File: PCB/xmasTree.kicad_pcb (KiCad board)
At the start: 2 copper layers, 183.5 x 138.9 mm, 37 parts, among them J1 USB_B_Micro, J2 Conn_01x05, J3 Conn_01x05, J4 Conn_01x05, J5 Conn_01x04, Q1 BSS138, U1 LD1117S33TR_SOT223, U2 ESP32-WROOM-32

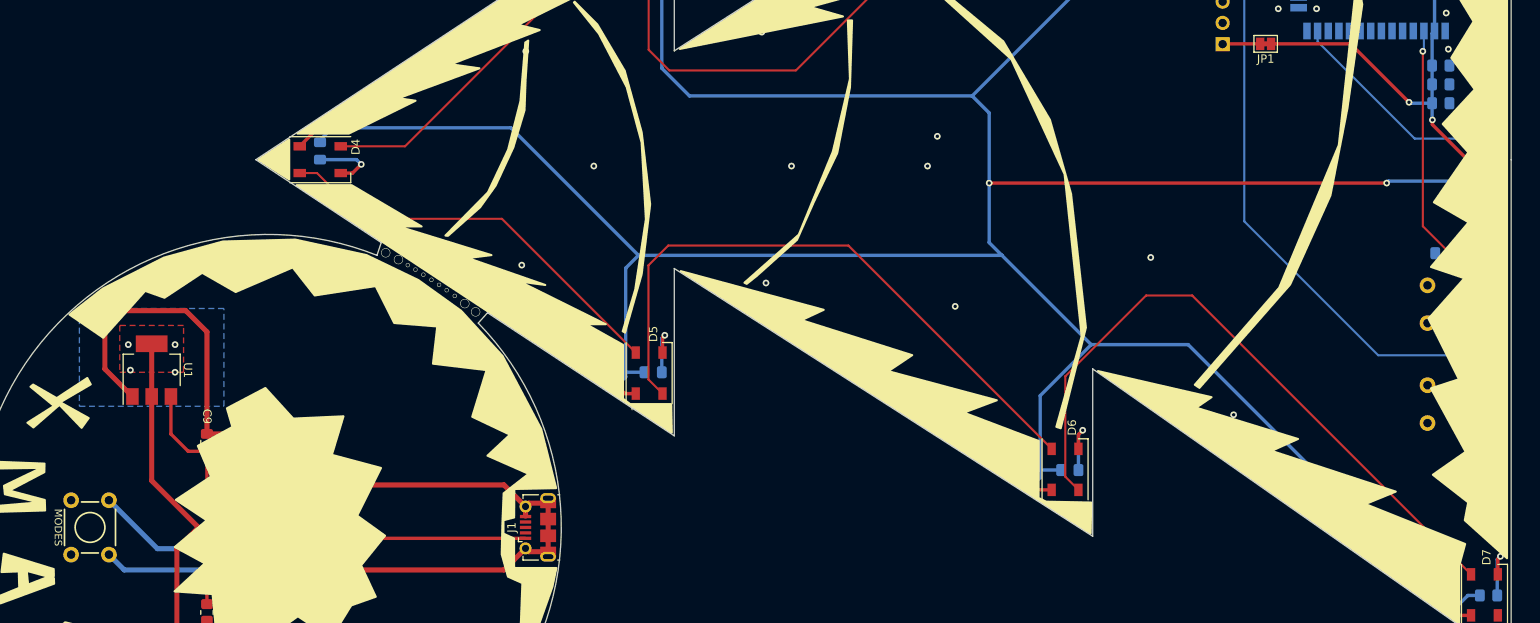
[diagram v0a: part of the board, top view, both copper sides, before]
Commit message: Updated to R2 4pin buttons were connected wrong. Swapped them to 2pin narrow version at the same time.
Signed-off-by: theloukou <lefteriskantakos@yahoo.com>
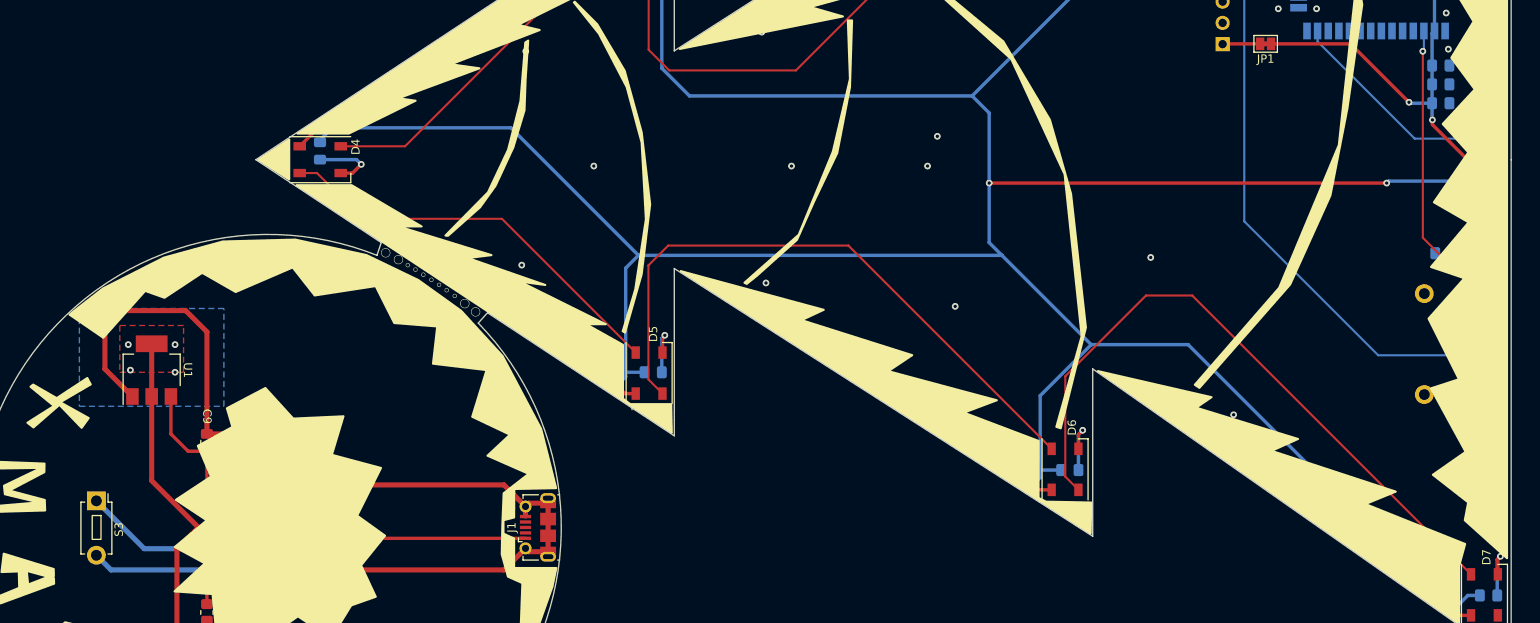
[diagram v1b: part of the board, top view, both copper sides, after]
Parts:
- S1: value RST -> SW_Push; footprint Switches:TACTILE_SWITCH_PTH_6.0MM -> Button_Switch_THT:SW_PUSH_1P1T_6x3.5mm_H4.3_APEM_MJTP1243
- S2: value BOOT -> SW_Push; footprint Switches:TACTILE_SWITCH_PTH_6.0MM -> Button_Switch_THT:SW_PUSH_1P1T_6x3.5mm_H4.3_APEM_MJTP1243
- S3: value MODES -> SW_Push; footprint Switches:TACTILE_SWITCH_PTH_6.0MM -> Button_Switch_THT:SW_PUSH_1P1T_6x3.5mm_H4.3_APEM_MJTP1243
- moved S3 3.27 mm to (54.6, 120.0)
- moved S1 3.14 mm to (219.8, 95.2)
- moved S2 3.09 mm to (219.8, 107.3)
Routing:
- net /EN: track 40.6 -> 42.7 mm
- net GND1: track 168.0 -> 169.5 mm
- net /MODES1: track 34.0 -> 35.5 mm
- net /00: track 84.2 -> 85.3 mm
